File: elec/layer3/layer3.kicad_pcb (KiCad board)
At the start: 2 copper layers, 125 x 125 mm, 53 parts, among them J10 Conn_01x05, J4 Conn_01x05, J8 XT30PW-M, J9 XT30PW-M, SW1 SW_SPDT_312, SW2 SW_SPDT_312, SW3 SW_SPDT_312, SW4 SW_SPDT_312, U1 CD74HC4067SM, U2 CD74HC4067SM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

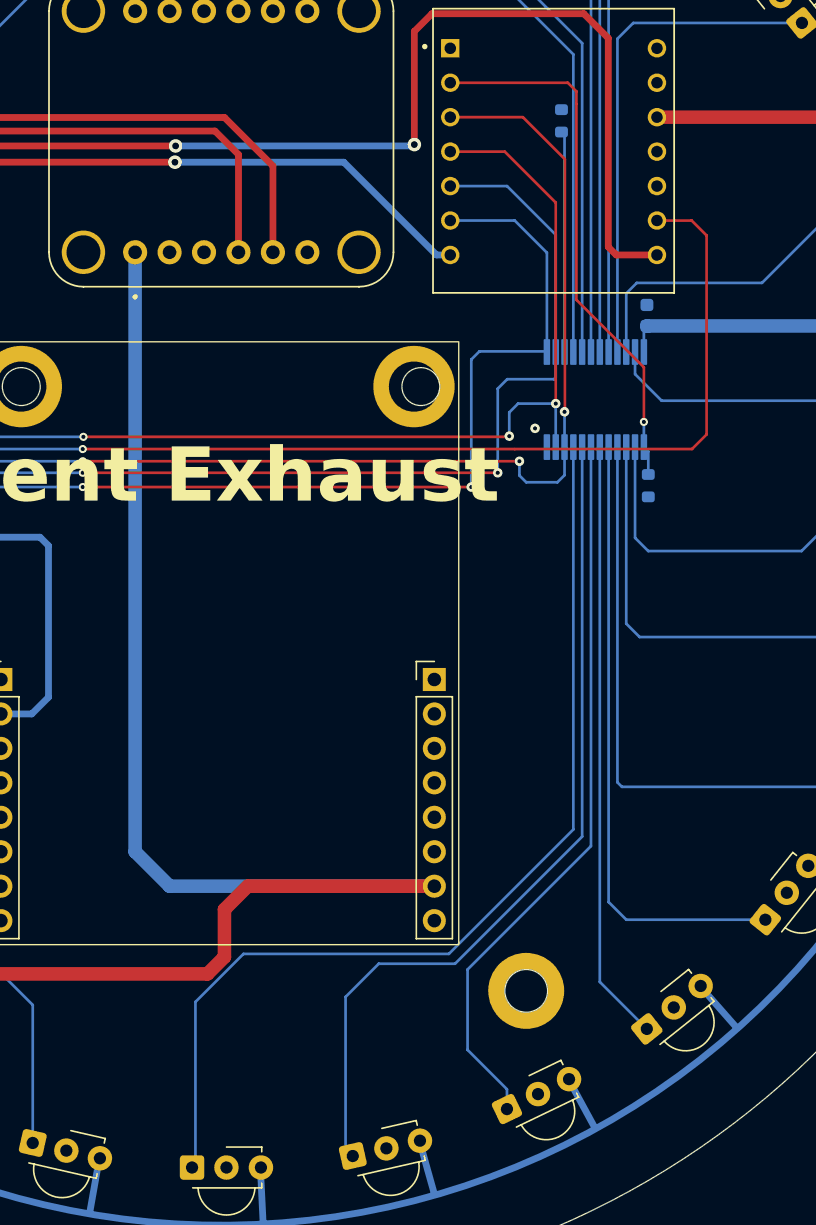
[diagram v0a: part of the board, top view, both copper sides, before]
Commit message: added res and cap
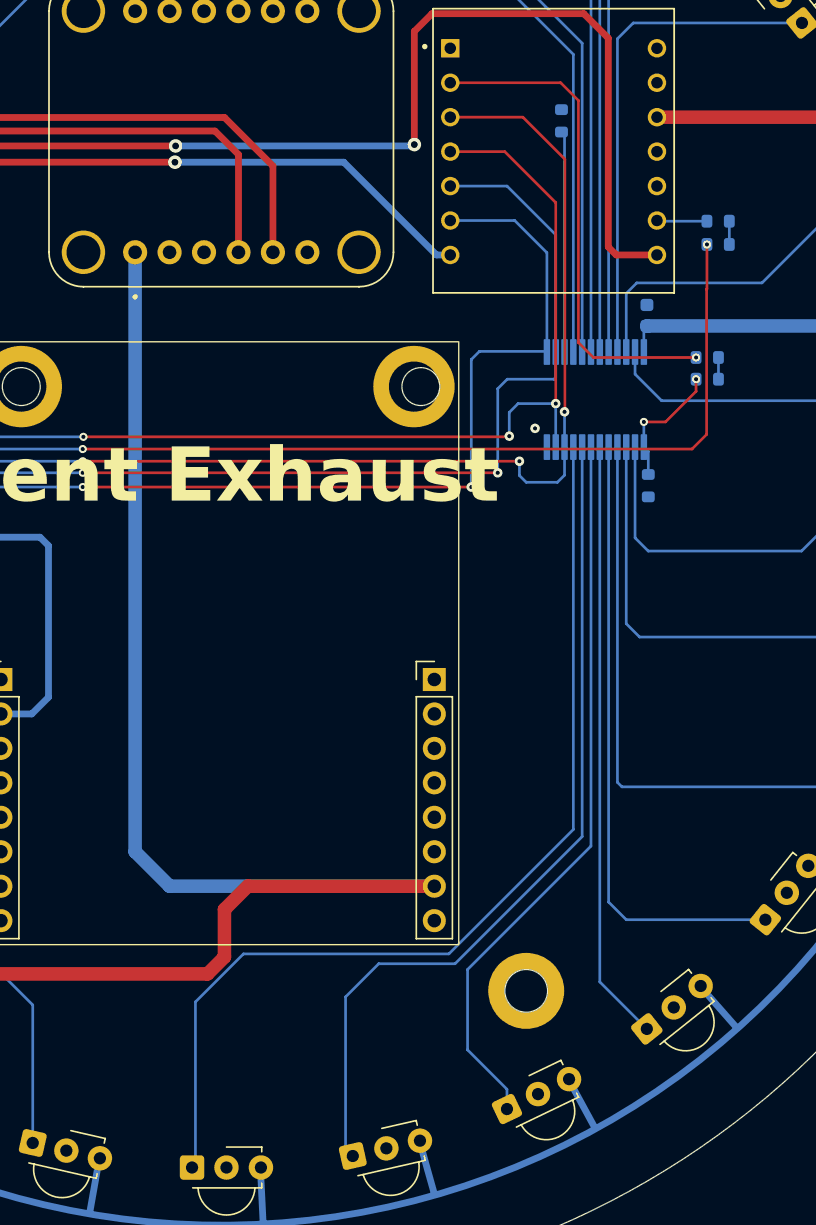
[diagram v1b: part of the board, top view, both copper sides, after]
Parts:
- added R5: 10k, Resistor_SMD:R_0603_1608Metric, B.Cu at (182.4, 89.9)
- added R6: 10uF, Resistor_SMD:R_0603_1608Metric, B.Cu at (182.4, 88.3)
- added R7: 10k, Resistor_SMD:R_0603_1608Metric, B.Cu at (183.2, 80.0)
- added R8: 10uF, Resistor_SMD:R_0603_1608Metric, B.Cu at (183.2, 78.2)
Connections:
- U5 pad 2: /Mux Com (17-32) -> Net-(U5-D1)
- U5 pad 9: /Mux Com (1-16) -> Net-(U5-D8)
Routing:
- net Net-(U5-D1): track 0.00 -> 37.0 mm, vias 0 -> 1
- net /Mux Com (17-32): track 40.1 -> 9.75 mm, vias 1 -> 2
- net /Mux Com (1-16): track 92.3 -> 87.5 mm, vias 1 -> 2
- net Net-(U5-D8): track 0.00 -> 3.78 mm
- net Net-(R7-Pad2): track 0.00 -> 1.72 mm
- net Net-(R5-Pad2): track 0.00 -> 1.60 mm

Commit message: l3 : sw change
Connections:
- SW1 pad 1: /Strat1 -> GND
- SW1 pad 2: GND -> /Strat1
- SW2 pad 1: /Strat2 -> GND
- SW2 pad 2: GND -> /Strat2
- SW3 pad 1: /Strat3 -> GND
- SW3 pad 2: GND -> /Strat3
- SW4 pad 1: /Strat4 -> GND
- SW4 pad 2: GND -> /Strat4
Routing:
- net /Strat3: track 42.0 -> 45.4 mm
- net /Strat2: track 62.0 -> 64.8 mm
- net /Strat1: track 59.8 -> 60.8 mm
- net /Strat4: track 39.4 -> 40.5 mm

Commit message: l3 : done
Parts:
- J8, J9: footprint L3:AMASS_XT30PW-M -> Connector_AMASS:AMASS_XT30UPB-M_1x02_P5.0mm_Vertical
- moved J8 9.18 mm to (109.8, 111.7), turned to 90 degrees
- moved J9 8.89 mm to (109.8, 95.8), turned to 90 degrees
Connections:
- U5 pad 12: +3V3 -> unconnected-(U5-VCC_3V3-Pad12)
- U5 pad 14: unconnected-(U5-VUSB-Pad14) -> +5V
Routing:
- net +5V: track 144.6 -> 235.4 mm
- net +3V3: track 98.6 -> 83.3 mm
- net /IR9: track 29.0 -> 30.6 mm
- net /Mux Com (17-32): track 9.75 -> 10.9 mm
- net /IR8: track 32.2 -> 31.5 mm
